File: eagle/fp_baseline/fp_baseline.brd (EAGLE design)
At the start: 95 x 24.7 mm, 2 parts

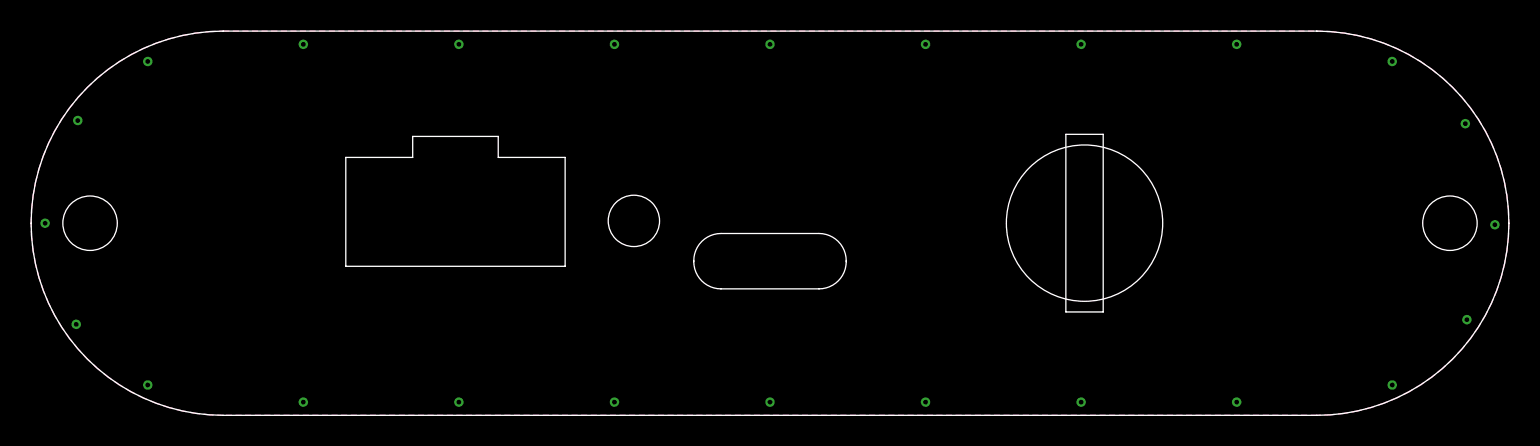
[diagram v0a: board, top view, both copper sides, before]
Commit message: Updates for JS220 first production build.
* Updated back panel for production build.
  * Increased USB hole size by 0.2 mm in left, right, and up directions
  * Bumped rev from C to D.
* Added additional boards:
  * fb_usb2_ba: USB 2.0 B/A connector
  * fp_bnc: BNC & 0.1" headers
  * fp_js110: Safety banana jacks configured like the JS110.
  * fp_baseline: Starting point for creating new boards in Eagle.
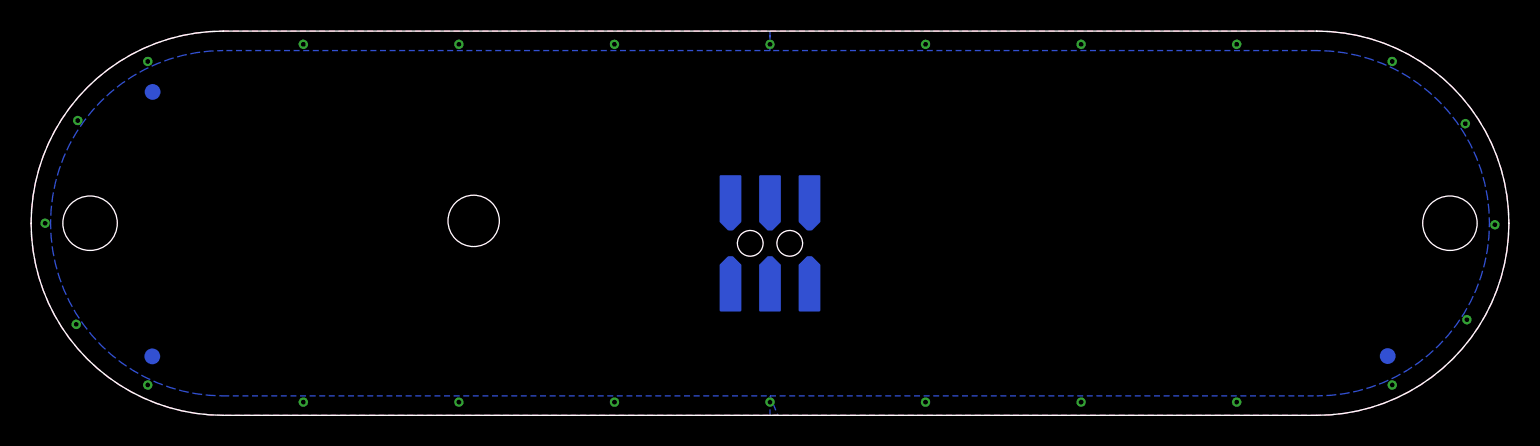
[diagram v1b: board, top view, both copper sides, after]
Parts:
- added FUD1, FUD2, FUD3: FIDUCIAL_1MM, jetperch:FIDUCIAL_1MM_2MM
- added J5: TSM-103-01-S-DV-A, jetperch:CONN_0.1_3X2_MSA
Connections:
- new net I+: J5.1, J5.2
- new net I-: J5.3, J5.4
- new net V+: J5.6
- new net V-: J5.5
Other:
- outline, holes or cut-outs redrawn
- board text added: "2x holes"
- board text added: "Isolated ±48V max to USB ground"
- board text added: "Part number Description"
- board text added: "Sensor Status"
- board text removed: "Controller Status"
- board text removed: "GPIO"
- board text removed: "GPIO and trigger are referenced to USB ground"
- board text removed: "OUT0 GND IN2 IN0 Vref"
- board text removed: "OUT1 GND IN3 IN1 GND"
- board text removed: "Out: 3.3V, 50 Ω In: TTL & 3.3V compatible"
- board text removed: "Trigger"
- board text removed: "USB"
- board text removed: "js220_ep_pcb_revC JS220 End Panel, Rev D 2022 Jetperch LLC"
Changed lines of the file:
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@@
 <board>
 <plain>
-<text x="47.5" y="20.2" size="1.27" layer="26" font="vector" ratio="20" rot="MR0" align="center">js220_ep_pcb_revC
-JS220 End Panel, Rev D
-2022 Jetperch LLC</text>
+<text x="47.5" y="20.2" size="1.27" layer="26" font="vector" ratio="20" rot="MR0" align="center">Part number
+Description</text>
 <dimension x1="0" y1="12.35" x2="95" y2="12.35" x3="47.5" y3="40.64" textsize="1.778" layer="47" dtype="horizontal"/>
-<dimension x1="12.35" y1="0" x2="12.35" y2="24.7" x3="-6.35" y3="12.35" textsize="1.778" layer="47" dtype="vertical"/>
-<dimension x1="38.75" y1="12.35" x2="47.5" y2="26.6" x3="43.125" y3="28.984990625" textsize="1.778" layer="47" dtype="horizontal" precision="3"/>
-<dimension x1="47.5" y1="26.6" x2="27.28" y2="12.5" x3="37.39" y3="33.21" textsize="1.778" layer="47" dtype="horizontal"/>
+<dimension x1="12.35" y1="0" x2="12.35" y2="24.7" x3="-17.35" y3="12.35" textsize="1.778" layer="47" dtype="vertical"/>
+<dimension x1="47.5" y1="26.6" x2="28.45" y2="12.5" x3="37.975" y3="33.21" textsize="1.778" layer="47" dtype="horizontal"/>
 <dimension x1="0" y1="26.6" x2="47.5" y2="26.6" x3="23.75" y3="36.794990625" textsize="1.778" layer="47"/>
 <text x="43.18" y="-10.16" size="1.778" layer="153">All dimensions in millimeters</text>
 <wire x1="3" y1="8.68" x2="42" y2="8.68" width="0.254" layer="22"/>
-<wire x1="3" y1="7.78" x2="63" y2="7.78" width="0.127" layer="22" style="shortdash"/>
-<wire x1="4" y1="6.88" x2="64" y2="6.88" width="0.254" layer="22"/>
+<wire x1="3" y1="7.78" x2="44" y2="7.78" width="0.127" layer="22" style="shortdash"/>
+<wire x1="4" y1="6.88" x2="42" y2="6.88" width="0.254" layer="22"/>
 <wire x1="0" y1="12.35" x2="12.35" y2="0" width="0" layer="20" curve="90"/>
 <wire x1="12.35" y1="0" x2="82.65" y2="0" width="0" layer="20"/>
@@
 <wire x1="82.65" y1="24.7" x2="12.35" y2="24.7" width="0" layer="20"/>
 <wire x1="12.35" y1="24.7" x2="0" y2="12.35" width="0" layer="20" curve="90"/>
-<text x="38.75" y="17" size="1.27" layer="29" font="vector" ratio="20" align="center">Controller
+<text x="28.45" y="8" size="1.5" layer="29" font="vector" ratio="20" align="center">Sensor
 Status</text>
-<hole x="38.75" y="12.5" drill="3.3"/>
-<wire x1="74" y1="8.68" x2="92" y2="8.68" width="0.254" layer="22"/>
-<wire x1="72" y1="6.88" x2="91" y2="6.88" width="0.254" layer="22"/>
-<wire x1="53" y1="8.68" x2="62" y2="8.68" width="0.254" layer="22"/>
-<wire x1="73" y1="7.78" x2="92" y2="7.78" width="0.127" layer="22" style="shortdash"/>
-<dimension x1="47.5" y1="26.6" x2="67.72" y2="12.655" x3="57.61" y3="36" textsize="1.778" layer="47" dtype="horizontal" precision="3"/>
+<hole x="28.45" y="12.5" drill="3.3"/>
+<wire x1="53" y1="6.88" x2="91" y2="6.88" width="0.254" layer="22"/>
+<wire x1="51" y1="7.78" x2="92" y2="7.78" width="0.127" layer="22" style="shortdash"/>
 <polygon width="0.254" layer="30">
 <vertex x="47.5" y="0"/>
@@
 <vertex x="47.5" y="1.25"/>
 </polygon>
-<hole x="67.72" y="12.355" drill="10.05"/>
-<wire x1="66.52" y1="18.065" x2="68.92" y2="18.065" width="0" layer="20"/>
-<wire x1="68.92" y1="18.065" x2="68.92" y2="6.645" width="0" layer="20"/>
-<wire x1="68.92" y1="6.645" x2="66.52" y2="6.645" width="0" layer="20"/>
-<wire x1="66.52" y1="6.645" x2="66.52" y2="18.065" width="0" layer="20"/>
-<text x="47.5" y="13.6" size="2" layer="29" font="vector" ratio="20" align="center">USB</text>
-<text x="67.72" y="19.6" size="2" layer="29" font="vector" ratio="20" align="center">Trigger</text>
-<text x="67.72" y="3.5" size="1" layer="29" font="vector" ratio="20" distance="40" align="center">Out: 3.3V, 50 Ω
-In: TTL &amp; 3.3V compatible</text>
-<text x="47.5" y="3.5" size="1" layer="29" font="vector" ratio="20" align="center">GPIO and trigger are
-referenced to USB ground</text>
-<wire x1="20.23" y1="9.58" x2="34.33" y2="9.58" width="0" layer="20"/>
-<wire x1="34.33" y1="9.58" x2="34.33" y2="16.58" width="0" layer="20"/>
-<wire x1="34.33" y1="16.58" x2="30.03" y2="16.58" width="0" layer="20"/>
-<wire x1="30.03" y1="16.58" x2="30.03" y2="17.93" width="0" layer="20"/>
-<wire x1="30.03" y1="17.93" x2="24.53" y2="17.93" width="0" layer="20"/>
-<wire x1="24.53" y1="17.93" x2="24.53" y2="16.58" width="0" layer="20"/>
-<wire x1="24.53" y1="16.58" x2="20.23" y2="16.58" width="0" layer="20"/>
-<wire x1="20.23" y1="16.58" x2="20.23" y2="9.58" width="0" layer="20"/>
-<text x="27.28" y="3.5" size="2" layer="29" font="vector" ratio="20" align="center">GPIO</text>
-<text x="27.28" y="8.98" size="1.27" layer="29" font="vector" ratio="20" distance="100" rot="SR270" align="center-left">OUT1
-GND
-IN3
-IN1
-GND</text>
-<text x="27.28" y="18.54" size="1.27" layer="29" font="vector" ratio="20" distance="100" rot="SR270" align="center-right">OUT0
-GND
-IN2
-IN0
-Vref</text>
-<text x="17.573" y="-22.892" size="1.778" layer="153">Place all markings on back (including pcb order number).
+<wire x1="53" y1="8.68" x2="92" y2="8.68" width="0.254" layer="22"/>
+<text x="12.573" y="-24.892" size="1.778" layer="153">Place all markings on back (including pcb order number).
 Add flammability rating marking on back, such as 94V-0.
 The front-side surface is cosmetic - reject units with scratches and blemishes.</text>
-<wire x1="44.35" y1="11.69" x2="50.65" y2="11.69" width="0" layer="20"/>
-<wire x1="50.65" y1="11.69" x2="52.4" y2="9.94" width="0" layer="20" curve="-90"/>
-<wire x1="52.4" y1="9.94" x2="52.4" y2="9.88" width="0" layer="20"/>
-<wire x1="52.4" y1="9.88" x2="50.65" y2="8.13" width="0" layer="20" curve="-90"/>
-<wire x1="50.65" y1="8.13" x2="44.35" y2="8.13" width="0" layer="20"/>
-<wire x1="44.35" y1="8.13" x2="42.6" y2="9.88" width="0" layer="20" curve="-90"/>
-<wire x1="42.6" y1="9.88" x2="42.6" y2="9.94" width="0" layer="20"/>
-<wire x1="42.6" y1="9.94" x2="44.35" y2="11.69" width="0" layer="20" curve="-90"/>
+<dimension x1="0" y1="0" x2="0" y2="12.35" x3="-4.35" y3="6.175" textsize="1.778" layer="47" dtype="vertical"/>
+<dimension x1="28.45" y1="0" x2="28.45" y2="12.5" x3="-12.35" y3="6.25" textsize="1.778" layer="47" dtype="vertical"/>
+<text x="-11.2" y="6.1" size="0.9" layer="47" rot="R90" align="center">Sensor Status</text>
+<text x="-2.9" y="6.3" size="0.9" layer="47" rot="R90" align="center">2x holes</text>
+<text x="47.5" y="4.008" size="1.5" layer="29" font="vector" ratio="20" align="center">Isolated
+±48V max to USB ground</text>
 </plain>
 <attributes>
@@
 </autorouter>
 <elements>
+<element name="J5" library="jetperch" package="CONN_0.1_3X2_MSA" value="TSM-103-01-S-DV-A" x="47.5" y="11.0565" smashed="yes" rot="MR0">
+<attribute name="MPN" value="TSM-103-01-S-DV-A" x="47.5" y="11.0565" size="1.778" layer="28" rot="MR0" display="off"/>
+<attribute name="NAME" x="51.642" y="5.3865" size="0.8128" layer="26" font="vector" ratio="22" rot="MR0"/>
+<attribute name="POPULATE" value="1" x="47.5" y="11.0565" size="1.778" layer="28" rot="MR0" display="off"/>
+</element>
+<element name="FUD1" library="jetperch" package="FIDUCIAL_1MM_2MM" value="FIDUCIAL_1MM" x="7.79" y="3.79" smashed="yes" rot="MR0">
+<attribute name="POPULATE" value="0" x="7.79" y="3.79" size="1.778" layer="28" rot="MR0" display="off"/>
+</element>
+<element name="FUD2" library="jetperch" package="FIDUCIAL_1MM_2MM" value="FIDUCIAL_1MM" x="7.81" y="20.79" smashed="yes" rot="MR0">
+<attribute name="POPULATE" value="0" x="7.81" y="20.79" size="1.778" layer="28" rot="MR0" display="off"/>
+</element>
+<element name="FUD3" library="jetperch" package="FIDUCIAL_1MM_2MM" value="FIDUCIAL_1MM" x="87.21" y="3.81" smashed="yes" rot="MR0">
+<attribute name="POPULATE" value="0" x="87.21" y="3.81" size="1.778" layer="28" rot="MR0" display="off"/>
+</element>
 <element name="H1" library="jetperch" package="HOLE_3.5MM_NORESTRICT" value="HOLE_#6_NORESTRICT" x="3.79" y="12.35" smashed="yes">
 <attribute name="POPULATE" value="0" x="3.79" y="12.35" size="1.778" layer="27" display="off"/>
@@
 </elements>
 <signals>
+<signal name="I+">
+<contactref element="J5" pad="1"/>
+<contactref element="J5" pad="2"/>
+<wire x1="50.04" y1="8.5165" x2="50.04" y2="13.5965" width="0" layer="19" extent="16-16"/>
+</signal>
+<signal name="V-">
+<contactref element="J5" pad="5"/>
+</signal>
+<signal name="I-">
+<contactref element="J5" pad="4"/>
+<contactref element="J5" pad="3"/>
+<wire x1="47.5" y1="8.5165" x2="47.5" y2="13.5965" width="0" layer="19" extent="16-16"/>
+</signal>
 <signal name="CGND">
-<polygon width="0.254" layer="1" isolate="0.254">
+<polygon width="0.254" layer="1" isolate="0.508">
 <vertex x="12.35" y="24.7"/>
 <vertex x="82.65" y="24.7" curve="-90"/>
@@
 <via x="2.9" y="5.85" extent="1-16" drill="0.3048"/>
 <polygon width="0.254" layer="16" isolate="0.254">
+<vertex x="48" y="0"/>
+<vertex x="12.35" y="0" curve="-90"/>
+<vertex x="0" y="12.35" curve="-90"/>
 <vertex x="12.35" y="24.7"/>
+<vertex x="47.5" y="24.7"/>
+<vertex x="47.5" y="23.45"/>
+<vertex x="12.35" y="23.45" curve="90"/>
+<vertex x="1.25" y="12.35" curve="90"/>
+<vertex x="12.35" y="1.25"/>
+<vertex x="47.5" y="1.25"/>
+</polygon>
+<polygon width="0.254" layer="16" isolate="0.254">
+<vertex x="47.5" y="0"/>
+<vertex x="47.5" y="1.25"/>
+<vertex x="82.65" y="1.25" curve="90"/>
+<vertex x="93.75" y="12.35" curve="90"/>
+<vertex x="82.65" y="23.45"/>
+<vertex x="47.5" y="23.45"/>
+<vertex x="47.5" y="24.7"/>
 <vertex x="82.65" y="24.7" curve="-90"/>
 <vertex x="95" y="12.35" curve="-90"/>
 <vertex x="82.65" y="0"/>
-<vertex x="12.35" y="0" curve="-90"/>
-<vertex x="0" y="12.35" curve="-90"/>
-</polygon>
+</polygon>
+</signal>
+<signal name="V+">
+<contactref element="J5" pad="6"/>
 </signal>
 </signals>
